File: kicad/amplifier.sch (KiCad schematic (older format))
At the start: 11 parts, among them U4 GS8332-SR

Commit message: BOM ist nun fast fertig
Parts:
- R10: value 4k7 -> 3k3; PriceEUR (none) -> 0.01
- R11: value 33k -> 30k; PriceEUR (none) -> 0.01
- R12: renamed from R?R1; PriceEUR (none) -> 0.01
- R13: renamed from R12; value 33k -> 30k; PriceEUR (none) -> 0.01
- R9: value 4k7 -> 10k; PriceEUR (none) -> 0.01
- R?R1: renamed from R?R2; PriceEUR (none) -> 0.01
- U4: ManPartNr (none) -> GS8332-SR; Manufacturer (none) -> Gainsil; Notes (none) -> Zero-Drift 2 2.1V ~ 5.5V 20uA 350kHz 0.2 V/us SOP-8_150mil 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; PriceEUR (none) -> 0.3016; PriceForQty (none) -> 100; Weblink (none) -> https://lcsc.com/product-detail/Precision-OpAmps_Gainsil-GS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
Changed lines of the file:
@@
 P 6250 3450
 F 0 "R11" H 6320 3496 50  0000 L CNN
-F 1 "33k" H 6320 3405 50  0000 L CNN
+F 1 "30k" H 6320 3405 50  0000 L CNN
 F 2 "Resistor_SMD:R_1206_3216Metric" V 6180 3450 50  0001 C CNN
 F 3 "~" H 6250 3450 50  0001 C CNN
+F 4 "0.01" H 6250 3450 50  0001 C CNN "PriceEUR"
 	1    6250 3450
 	1    0    0    -1
 $EndComp
 $Comp
-L Device:R R?R1
+L Device:R R12
 U 1 1 608F3C13
 P 6250 3900
-F 0 "R?R1" H 6320 3946 50  0000 L CNN
+F 0 "R12" H 6320 3946 50  0000 L CNN
 F 1 "100R" H 6320 3855 50  0000 L CNN
 F 2 "Resistor_SMD:R_1206_3216Metric" V 6180 3900 50  0001 C CNN
 F 3 "~" H 6250 3900 50  0001 C CNN
+F 4 "0.01" H 6250 3900 50  0001 C CNN "PriceEUR"
 	1    6250 3900
 	1    0    0    -1
@@
 P 3750 3000
 F 0 "R9" V 3543 3000 50  0000 C CNN
-F 1 "4k7" V 3634 3000 50  0000 C CNN
+F 1 "10k" V 3634 3000 50  0000 C CNN
 F 2 "Resistor_SMD:R_1206_3216Metric" V 3680 3000 50  0001 C CNN
 F 3 "~" H 3750 3000 50  0001 C CNN
+F 4 "0.01" H 3750 3000 50  0001 C CNN "PriceEUR"
 	1    3750 3000
 	0    1    1    0
@@
 	5300 5300 4850 5300
 $Comp
-L Device:R R12
+L Device:R R13
 U 1 1 60A2E38C
 P 6250 5750
-F 0 "R12" H 6320 5796 50  0000 L CNN
-F 1 "33k" H 6320 5705 50  0000 L CNN
+F 0 "R13" H 6320 5796 50  0000 L CNN
+F 1 "30k" H 6320 5705 50  0000 L CNN
 F 2 "Resistor_SMD:R_1206_3216Metric" V 6180 5750 50  0001 C CNN
 F 3 "~" H 6250 5750 50  0001 C CNN
+F 4 "0.01" H 6250 5750 50  0001 C CNN "PriceEUR"
 	1    6250 5750
 	1    0    0    -1
 $EndComp
 $Comp
-L Device:R R?R2
+L Device:R R?R1
 U 1 1 60A2E392
 P 6250 6200
-F 0 "R?R2" H 6320 6246 50  0000 L CNN
+F 0 "R?R1" H 6320 6246 50  0000 L CNN
 F 1 "100R" H 6320 6155 50  0000 L CNN
 F 2 "Resistor_SMD:R_1206_3216Metric" V 6180 6200 50  0001 C CNN
 F 3 "~" H 6250 6200 50  0001 C CNN
+F 4 "0.01" H 6250 6200 50  0001 C CNN "PriceEUR"
 	1    6250 6200
 	1    0    0    -1
@@
 P 3800 5300
 F 0 "R10" V 3593 5300 50  0000 C CNN
-F 1 "4k7" V 3684 5300 50  0000 C CNN
+F 1 "3k3" V 3684 5300 50  0000 C CNN
 F 2 "Resistor_SMD:R_1206_3216Metric" V 3730 5300 50  0001 C CNN
 F 3 "~" H 3800 5300 50  0001 C CNN
+F 4 "0.01" H 3800 5300 50  0001 C CNN "PriceEUR"
 	1    3800 5300
 	0    1    1    0
@@
 F 4 "C157713" H 5600 5400 50  0001 C CNN "DistOrderNr"
 F 5 "LCSC" H 5600 5400 50  0001 C CNN "Distributor"
+F 6 "GS8332-SR" H 5600 5400 50  0001 C CNN "ManPartNr"
+F 7 "Gainsil" H 5600 5400 50  0001 C CNN "Manufacturer"
+F 8 "Zero-Drift 2 2.1V ~ 5.5V 20uA 350kHz 0.2 V/us SOP-8_150mil Precision OpAmps" H 5600 5400 50  0001 C CNN "Notes"
+F 9 "0.3016" H 5600 5400 50  0001 C CNN "PriceEUR"
+F 10 "100" H 5600 5400 50  0001 C CNN "PriceForQty"
+F 11 "https://lcsc.com/product-detail/Precision-OpAmps_Gainsil-GS8332-SR_C157713.html" H 5600 5400 50  0001 C CNN "Weblink"
 	2    5600 5400
 	1    0    0    -1
@@
 F 4 "C157713" H 5600 3100 50  0001 C CNN "DistOrderNr"
 F 5 "LCSC" H 5600 3100 50  0001 C CNN "Distributor"
+F 6 "GS8332-SR" H 5600 3100 50  0001 C CNN "ManPartNr"
+F 7 "Gainsil" H 5600 3100 50  0001 C CNN "Manufacturer"
+F 8 "Zero-Drift 2 2.1V ~ 5.5V 20uA 350kHz 0.2 V/us SOP-8_150mil Precision OpAmps" H 5600 3100 50  0001 C CNN "Notes"
+F 9 "0.3016" H 5600 3100 50  0001 C CNN "PriceEUR"
+F 10 "100" H 5600 3100 50  0001 C CNN "PriceForQty"
+F 11 "https://lcsc.com/product-detail/Precision-OpAmps_Gainsil-GS8332-SR_C157713.html" H 5600 3100 50  0001 C CNN "Weblink"
 	1    5600 3100
 	1    0    0    -1
@@
 F 4 "C157713" H 5600 3100 50  0001 C CNN "DistOrderNr"
 F 5 "LCSC" H 5600 3100 50  0001 C CNN "Distributor"
+F 6 "GS8332-SR" H 5600 3100 50  0001 C CNN "ManPartNr"
+F 7 "Gainsil" H 5600 3100 50  0001 C CNN "Manufacturer"
+F 8 "Zero-Drift 2 2.1V ~ 5.5V 20uA 350kHz 0.2 V/us SOP-8_150mil Precision OpAmps" H 5600 3100 50  0001 C CNN "Notes"
+F 9 "0.3016" H 5600 3100 50  0001 C CNN "PriceEUR"
+F 10 "100" H 5600 3100 50  0001 C CNN "PriceForQty"
+F 11 "https://lcsc.com/product-detail/Precision-OpAmps_Gainsil-GS8332-SR_C157713.html" H 5600 3100 50  0001 C CNN "Weblink"
 	3    5600 3100
 	1    0    0    -1

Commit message: BOM Fertig, 3D auch fast fertig. Ein paar Footrpints fehlen noch.
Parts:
- removed C7: 10n, Capacitor_SMD:C_1206_3216Metric, symbol Device:C
- removed R10: 3k3, Resistor_SMD:R_1206_3216Metric, symbol Device:R
- added C17: 100n, Capacitor_SMD:C_1206_3216Metric, symbol Device:C
- added D5: BAV99, Package_TO_SOT_SMD:SOT-23, symbol Diode:BAV99
- added R19: 100k, Resistor_SMD:R_1206_3216Metric, symbol Device:R
- added R20: 1k, Resistor_SMD:R_1206_3216Metric, symbol Device:R
- R21: renamed from R9; DistOrderNr (none) -> C118075; Distributor (none) -> LCSC
- R22: renamed from R11; DistOrderNr (none) -> C137314; Distributor (none) -> LCSC
- R23: renamed from R12; DistOrderNr (none) -> C113307; Distributor (none) -> LCSC; ManPartNr (none) -> RC1206JR-07100RL; Manufacturer (none) -> YAGEO; Notes (none) -> 100Ω ±5% 0.25W ±100ppm/℃ 1206 Chip Resistor; PriceEUR 0.01 -> 0.0037; PriceForQty (none) -> 500
- R24: renamed from R13; DistOrderNr (none) -> C137314; Distributor (none) -> LCSC
- R25: renamed from R?R1; DistOrderNr (none) -> C113307; Distributor (none) -> LCSC; ManPartNr (none) -> RC1206JR-07100RL; Manufacturer (none) -> YAGEO; Notes (none) -> 100Ω ±5% 0.25W ±100ppm/℃ 1206 Chip Resistor; PriceEUR 0.01 -> 0.0037; PriceForQty (none) -> 500
- U6: renamed from U4; footprint Package_SO:SO-8_3.9x4.9mm_P1.27mm -> Package_SO:SOIC-8_3.9x4.9mm_P1.27mm
- renumbered C6 to C18, C8 to C19, D2 to D6
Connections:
- wire segments 41 -> 52
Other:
- note added: "Pullup zum Detektieren\neiner fehlenden Lötspitze."
- note added: "Tau = 100us"
- note removed: "Tau = 47us"

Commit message: kleinere Updates im Schaltplan
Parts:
- D5, D6: symbol Diode:BAV99 -> jbc-miniregler-rescue:BAV99-Diode
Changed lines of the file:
@@
 	6000 2500 5900 2500
 $Comp
-L Diode:BAV99 D6
+L jbc-miniregler-rescue:BAV99-Diode D6
 U 2 1 608F0A12
 P 4350 3300
@@
 $EndComp
 $Comp
-L Diode:BAV99 D6
+L jbc-miniregler-rescue:BAV99-Diode D6
 U 1 1 608F1916
 P 4150 3300
@@
 Pullup zum Detektieren\neiner fehlenden Lötspitze.
 $Comp
-L Diode:BAV99 D5
+L jbc-miniregler-rescue:BAV99-Diode D5
 U 2 1 60B76F24
 P 3950 5550
@@
 $EndComp
 $Comp
-L Diode:BAV99 D5
+L jbc-miniregler-rescue:BAV99-Diode D5
 U 1 1 60B76F32
 P 3750 5550

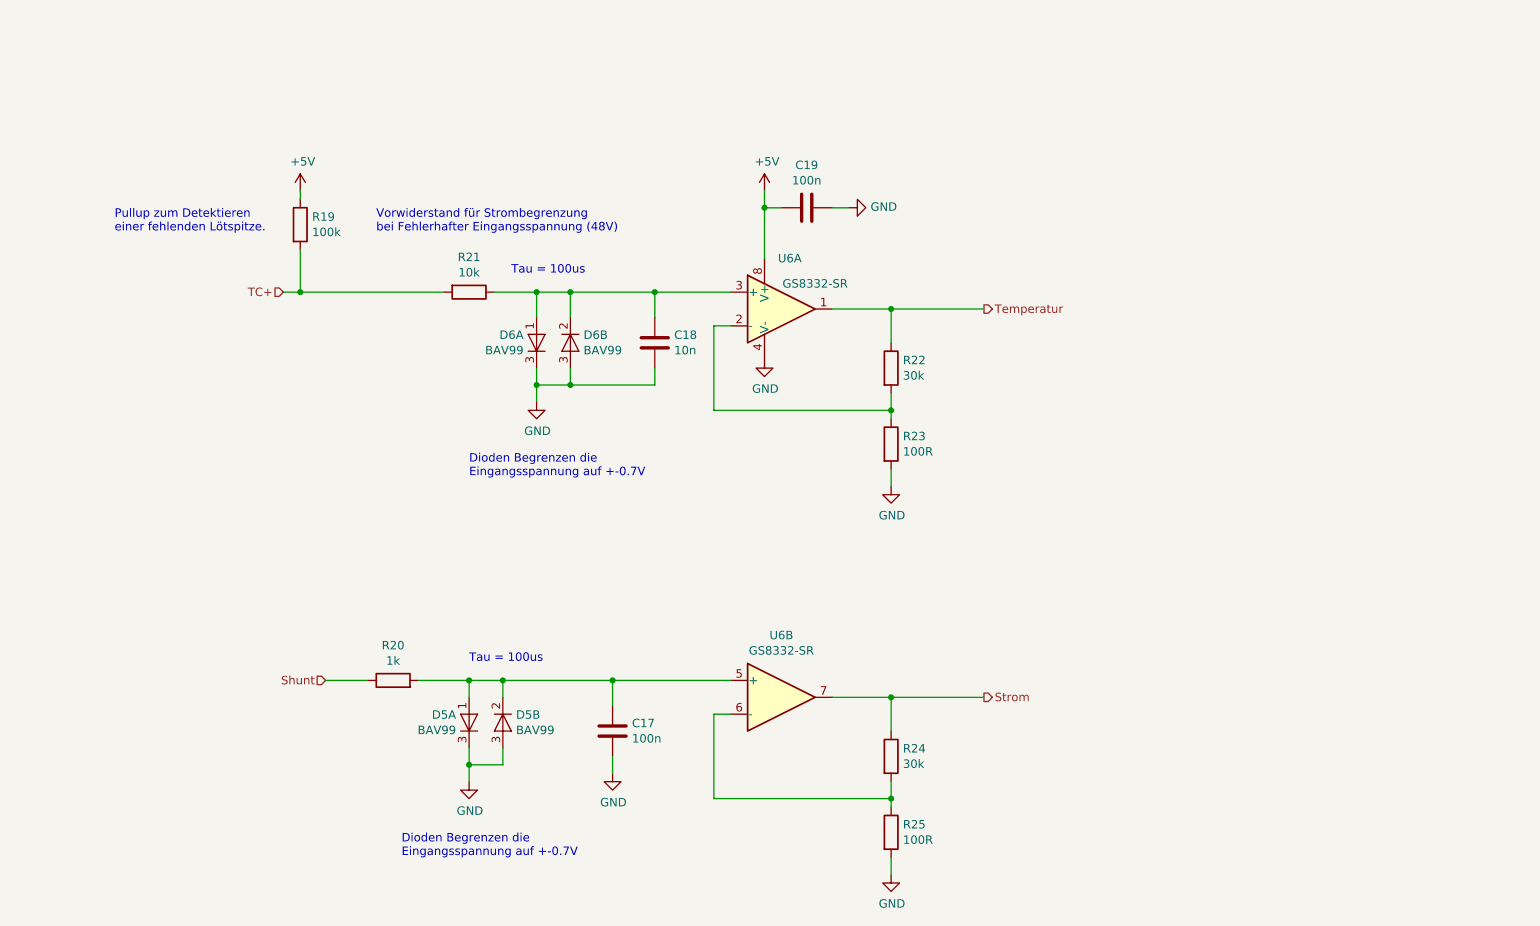
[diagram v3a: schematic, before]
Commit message: OPV-Polaritätsoption, Zusatzfilter und Strombegrenzung
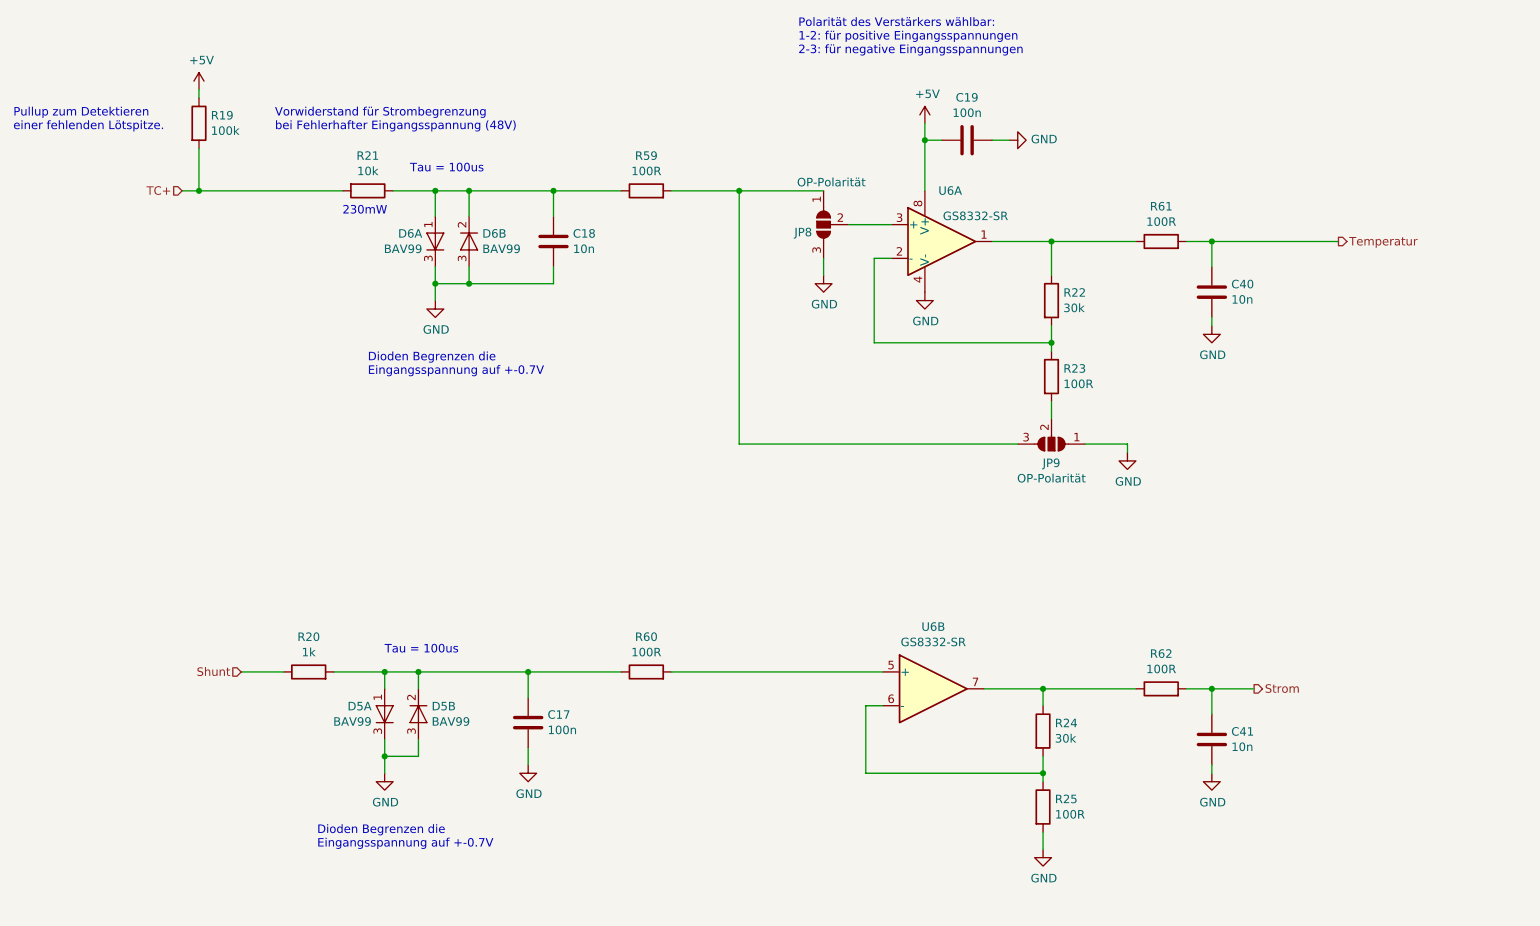
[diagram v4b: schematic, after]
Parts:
- added C40, C41: 10n, Capacitor_SMD:C_1206_3216Metric, symbol Device:C
- added JP8, JP9: OP-Polarität, Jumper:SolderJumper-3_P2.0mm_Open_TrianglePad1.0x1.5mm_NumberLabels, symbol Jumper:SolderJumper_3_Open
- added R59, R60, R61, R62: 100R, Resistor_SMD:R_1206_3216Metric, symbol Device:R
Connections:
- net GND: now also C40.2, C41.2, JP8.3 (B), JP9.1 (A); no longer R23.2
- net Strom: now also C41.1, R62.2; no longer R24.1, U6.7
- net Temperatur: now also C40.1, R61.2; no longer R22.1, U6.1
- net at C18.1, D6.1 (A), D6.2 (K)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: now also R59.1; no longer U6.3 (+)
- net at C17.2, D5.1 (A), D5.2 (K)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: now also R60.1; no longer U6.5 (+)
- new net: R22.1, R61.1, U6.1
- new net: JP8.2 (C), U6.3 (+)
- new net: JP9.2 (C), R23.2
- new net: R60.2, U6.5 (+)
- new net: R24.1, R62.1, U6.7
- new net: JP8.1 (A), JP9.3 (B), R59.2
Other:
- note added: "230mW"
- note added: "Polarität des Verstärkers wählbar:\n1-2: für positive Eingangsspannungen\n2-3: für negative Eingangsspannungen"
- moved on the sheet: C17, C18, C19, D5A, D5B, D6A, D6B, R19, R20, R21, R22, R23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

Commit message: Neu: Spannungsreferenz TL431, Laout Fertig, TODO: Labels
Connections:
- net GND: now also D5.1 (A), D5.2 (K), D6.1 (A), D6.2 (K); no longer D5.3 (A), D5.3 (K), D6.3 (A), D6.3 (K)
- net at C18.1, R21.1, R59.1: now also D6.3 (A), D6.3 (K); no longer D6.1 (A), D6.2 (K)
- net at C17.2, R20.2, R60.1: now also D5.3 (A), D5.3 (K); no longer D5.1 (A), D5.2 (K)
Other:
- moved on the sheet: D5A, D5B, D6A, D6B
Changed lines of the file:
@@
 L jbc-miniregler-rescue:BAV99-Diode D6
 U 2 1 608F0A12
+P 3550 2700
+F 0 "D6" V 3504 2778 50  0000 L CNN
+F 1 "BAV99" V 3595 2778 50  0000 L CNN
+F 2 "Package_TO_SOT_SMD:SOT-23" H 3550 2550 50  0001 C CNN
+F 3 "https://assets.nexperia.com/documents/data-sheet/BAV99_SER.pdf" H 3550 2800 50  0001 C CNN
+F 4 "C181111" H 3550 2700 50  0001 C CNN "DistOrderNr"
+F 5 "LCSC" H 3550 2700 50  0001 C CNN "Distributor"
+F 6 "BAV99" H 3550 2700 50  0001 C CNN "ManPartNr"
+F 7 "Guangdong Hottech" H 3550 2700 50  0001 C CNN "Manufacturer"
+F 8 "70V 200mA 1.25V @ 150mA 6ns SOT-23 Switching Diode" H 3550 2700 50  0001 C CNN "Notes"
+F 9 "0.0073" H 3550 2700 50  0001 C CNN "PriceEUR"
+F 10 "500" H 3550 2700 50  0001 C CNN "PriceForQty"
+F 11 "https://lcsc.com/product-detail/Switching-Diode_BAV99-chip0-23_C181111.html" H 3550 2700 50  0001 C CNN "Weblink"
+	2    3550 2700
+	0    -1   -1   0
+$EndComp
+$Comp
+L jbc-miniregler-rescue:BAV99-Diode D6
+U 1 1 608F1916
 P 3750 2700
-F 0 "D6" V 3704 2778 50  0000 L CNN
-F 1 "BAV99" V 3795 2778 50  0000 L CNN
+F 0 "D6" V 3796 2777 50  0000 L CNN
+F 1 "BAV99" V 3705 2777 50  0000 L CNN
 F 2 "Package_TO_SOT_SMD:SOT-23" H 3750 2550 50  0001 C CNN
 F 3 "https://assets.nexperia.com/documents/data-sheet/BAV99_SER.pdf" H 3750 2800 50  0001 C CNN
@@
 F 10 "500" H 3750 2700 50  0001 C CNN "PriceForQty"
 F 11 "https://lcsc.com/product-detail/Switching-Diode_BAV99-chip0-23_C181111.html" H 3750 2700 50  0001 C CNN "Weblink"
-	2    3750 2700
+	1    3750 2700
 	0    1    1    0
-$EndComp
-$Comp
-L jbc-miniregler-rescue:BAV99-Diode D6
-U 1 1 608F1916
-P 3550 2700
-F 0 "D6" V 3596 2777 50  0000 L CNN
-F 1 "BAV99" V 3505 2777 50  0000 L CNN
-F 2 "Package_TO_SOT_SMD:SOT-23" H 3550 2550 50  0001 C CNN
-F 3 "https://assets.nexperia.com/documents/data-sheet/BAV99_SER.pdf" H 3550 2800 50  0001 C CNN
-F 4 "C181111" H 3550 2700 50  0001 C CNN "DistOrderNr"
-F 5 "LCSC" H 3550 2700 50  0001 C CNN "Distributor"
-F 6 "BAV99" H 3550 2700 50  0001 C CNN "ManPartNr"
-F 7 "Guangdong Hottech" H 3550 2700 50  0001 C CNN "Manufacturer"
-F 8 "70V 200mA 1.25V @ 150mA 6ns SOT-23 Switching Diode" H 3550 2700 50  0001 C CNN "Notes"
-F 9 "0.0073" H 3550 2700 50  0001 C CNN "PriceEUR"
-F 10 "500" H 3550 2700 50  0001 C CNN "PriceForQty"
-F 11 "https://lcsc.com/product-detail/Switching-Diode_BAV99-chip0-23_C181111.html" H 3550 2700 50  0001 C CNN "Weblink"
-	1    3550 2700
-	0    -1   -1   0
 $EndComp
 Wire Wire Line
@@
 L jbc-miniregler-rescue:BAV99-Diode D5
 U 1 1 60B76F32
+P 3450 5500
+F 0 "D5" V 3496 5577 50  0000 L CNN
+F 1 "BAV99" V 3405 5577 50  0000 L CNN
+F 2 "Package_TO_SOT_SMD:SOT-23" H 3450 5350 50  0001 C CNN
+F 3 "https://assets.nexperia.com/documents/data-sheet/BAV99_SER.pdf" H 3450 5600 50  0001 C CNN
+F 4 "C181111" H 3450 5500 50  0001 C CNN "DistOrderNr"
+F 5 "LCSC" H 3450 5500 50  0001 C CNN "Distributor"
+F 6 "BAV99" H 3450 5500 50  0001 C CNN "ManPartNr"
+F 7 "Guangdong Hottech" H 3450 5500 50  0001 C CNN "Manufacturer"
+F 8 "70V 200mA 1.25V @ 150mA 6ns SOT-23 Switching Diode" H 3450 5500 50  0001 C CNN "Notes"
+F 9 "0.0073" H 3450 5500 50  0001 C CNN "PriceEUR"
+F 10 "500" H 3450 5500 50  0001 C CNN "PriceForQty"
+F 11 "https://lcsc.com/product-detail/Switching-Diode_BAV99-chip0-23_C181111.html" H 3450 5500 50  0001 C CNN "Weblink"
+	1    3450 5500
+	0    1    1    0
+$EndComp
+$Comp
+L jbc-miniregler-rescue:BAV99-Diode D5
+U 2 1 60B76F24
 P 3250 5500
-F 0 "D5" V 3296 5577 50  0000 L CNN
-F 1 "BAV99" V 3205 5577 50  0000 L CNN
+F 0 "D5" V 3204 5578 50  0000 L CNN
+F 1 "BAV99" V 3295 5578 50  0000 L CNN
 F 2 "Package_TO_SOT_SMD:SOT-23" H 3250 5350 50  0001 C CNN
 F 3 "https://assets.nexperia.com/documents/data-sheet/BAV99_SER.pdf" H 3250 5600 50  0001 C CNN
@@
 F 10 "500" H 3250 5500 50  0001 C CNN "PriceForQty"
 F 11 "https://lcsc.com/product-detail/Switching-Diode_BAV99-chip0-23_C181111.html" H 3250 5500 50  0001 C CNN "Weblink"
-	1    3250 5500
+	2    3250 5500
 	0    -1   -1   0
 $EndComp
-$Comp
-L jbc-miniregler-rescue:BAV99-Diode D5
-U 2 1 60B76F24
-P 3450 5500
-F 0 "D5" V 3404 5578 50  0000 L CNN
-F 1 "BAV99" V 3495 5578 50  0000 L CNN
-F 2 "Package_TO_SOT_SMD:SOT-23" H 3450 5350 50  0001 C CNN
-F 3 "https://assets.nexperia.com/documents/data-sheet/BAV99_SER.pdf" H 3450 5600 50  0001 C CNN
-F 4 "C181111" H 3450 5500 50  0001 C CNN "DistOrderNr"
-F 5 "LCSC" H 3450 5500 50  0001 C CNN "Distributor"
-F 6 "BAV99" H 3450 5500 50  0001 C CNN "ManPartNr"
-F 7 "Guangdong Hottech" H 3450 5500 50  0001 C CNN "Manufacturer"
-F 8 "70V 200mA 1.25V @ 150mA 6ns SOT-23 Switching Diode" H 3450 5500 50  0001 C CNN "Notes"
-F 9 "0.0073" H 3450 5500 50  0001 C CNN "PriceEUR"
-F 10 "500" H 3450 5500 50  0001 C CNN "PriceForQty"
-F 11 "https://lcsc.com/product-detail/Switching-Diode_BAV99-chip0-23_C181111.html" H 3450 5500 50  0001 C CNN "Weblink"
-	2    3450 5500
-	0    1    1    0
-$EndComp
-Wire Wire Line
+Wire Wire Line
